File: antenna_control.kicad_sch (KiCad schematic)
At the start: 26 parts, among them J7 G125-MH11005L1P, J9 FTSH-105-01-L-DV-K, Q12 DMP2160UWQ-7, Q13 DMP3056LDM-7, U46 M0L1228QRGERQ1

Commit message: Add licensing
Use CERN-OHL-W version 2

Signed-off-by: Corey Minyard <corey@minyard.net>
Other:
- company: (none) -> AMSAT-NA
- title: (none) -> Processor for Interfaces to the Antenna Controller
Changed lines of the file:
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@@
 	(generator_version "10.0")
 	(paper "A4")
+	(title_block
+		(title "Processor for Interfaces to the Antenna Controller")
+		(date "2026-08-20")
+		(rev "4.0")
+		(company "AMSAT-NA")
+		(comment 1 "AE5KM")
+		(comment 2 "Copyright Corey Minyard, 2026")
+		(comment 3 "Licensed under CERN-OHL-W version 2")
+	)
 	(text "Can also be used as ADC channel 14 or BSL_Invoke"
 		(exclude_from_sim no)

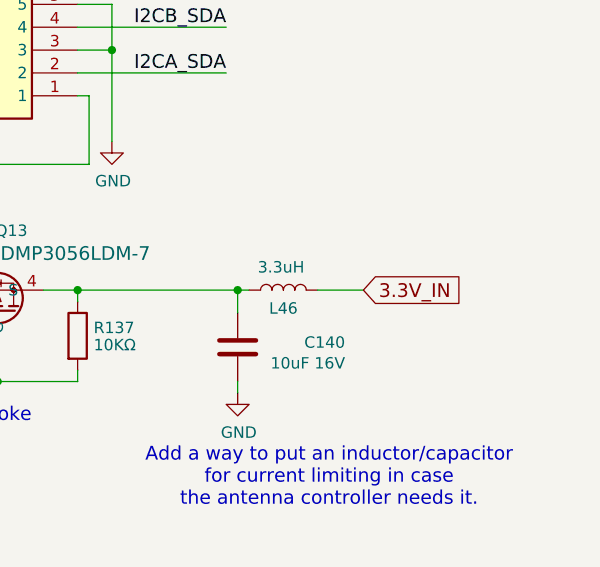
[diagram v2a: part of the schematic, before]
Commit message: Replace the metal allow inductors with ones that can be space-rated
Coilcraft had some space-rated and non-space-rated parts that had
equivalent footprints, which was handy.

Signed-off-by: Corey Minyard <corey@minyard.net>
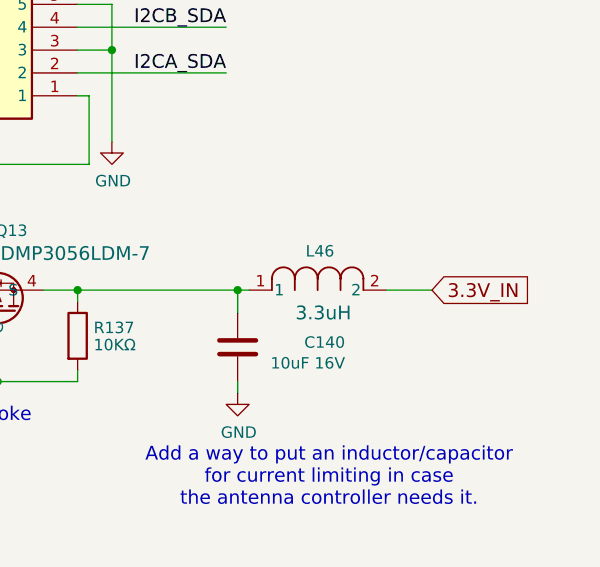
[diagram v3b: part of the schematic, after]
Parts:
- L46: footprint Inductor_SMD:L_1210_3225Metric_Pad1.42x2.65mm_HandSolder -> PacSatDev_misc:IND_EPL2010_COC; symbol Device:L -> PACSAT_DEV_misc:EPL2010
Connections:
- net 3.3V_IN: now also L46.2; no longer L46.1
- net at C140.1, Q13.4 (S), R137.1: now also L46.1; no longer L46.2
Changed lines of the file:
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@@
 	)
 	(junction
-		(at 247.65 68.58)
-		(diameter 0)
-		(color 0 0 0 0)
-	)
-	(junction
 		(at 134.62 137.16)
 		(diameter 0)
@@
 	)
 	(junction
+		(at 247.65 68.58)
+		(diameter 0)
+		(color 0 0 0 0)
+	)
+	(junction
 		(at 73.66 95.25)
 		(diameter 0)
@@
 	(wire
 		(pts
-			(xy 261.62 68.58) (xy 256.54 68.58)
+			(xy 269.24 68.58) (xy 264.16 68.58)
 		)
 		(stroke
@@
 	(global_label "3.3V_IN"
 		(shape input)
-		(at 261.62 68.58 0)
+		(at 269.24 68.58 0)
 		(fields_autoplaced yes)
 		(effects
@@
 		)
 		(property "Intersheetrefs" "${INTERSHEET_REFS}"
-			(at 272.835 68.58 0)
+			(at 280.455 68.58 0)
 			(hide yes)
 			(show_name no)
@@
 	)
 	(symbol
-		(lib_id "Device:L")
-		(at 252.73 68.58 270)
-		(mirror x)
+		(lib_id "PACSAT_DEV_misc:EPL2010")
+		(at 264.16 68.58 0)
+		(mirror y)
 		(unit 1)
 		(body_style 1)
@@
 		(dnp no)
 		(property "Reference" "L46"
-			(at 252.73 70.612 90)
+			(at 256.794 64.262 0)
 			(show_name no)
 			(do_not_autoplace no)
@@
 		)
 		(property "Value" "3.3uH"
-			(at 252.476 66.04 90)
+			(at 257.175 71.12 0)
 			(show_name no)
 			(do_not_autoplace no)
 			(effects
 				(font
-					(size 1.27 1.27)
+					(size 1.524 1.524)
 				)
 			)
 		)
-		(property "Footprint" "Inductor_SMD:L_1210_3225Metric_Pad1.42x2.65mm_HandSolder"
-			(at 252.73 68.58 0)
+		(property "Footprint" "PacSatDev_misc:IND_EPL2010_COC"
+			(at 264.16 68.58 0)
 			(hide yes)
 			(show_name no)
@@
 				(font
 					(size 1.27 1.27)
+					(italic yes)
 				)
 			)
 		)
-		(property "Datasheet" ""
-			(at 252.73 68.58 0)
+		(property "Datasheet" "https://www.coilcraft.com/getmedia/bdfddf40-0df1-48c7-a72c-6d6f57760a03/epl2010.pdf"
+			(at 264.16 68.58 0)
 			(hide yes)
 			(show_name no)
@@
 				(font
 					(size 1.27 1.27)
+					(italic yes)
 				)
 			)
 		)
 		(property "Description" ""
-			(at 252.73 68.58 0)
+			(at 264.16 68.58 0)
+			(hide yes)
 			(show_name no)
 			(do_not_autoplace no)

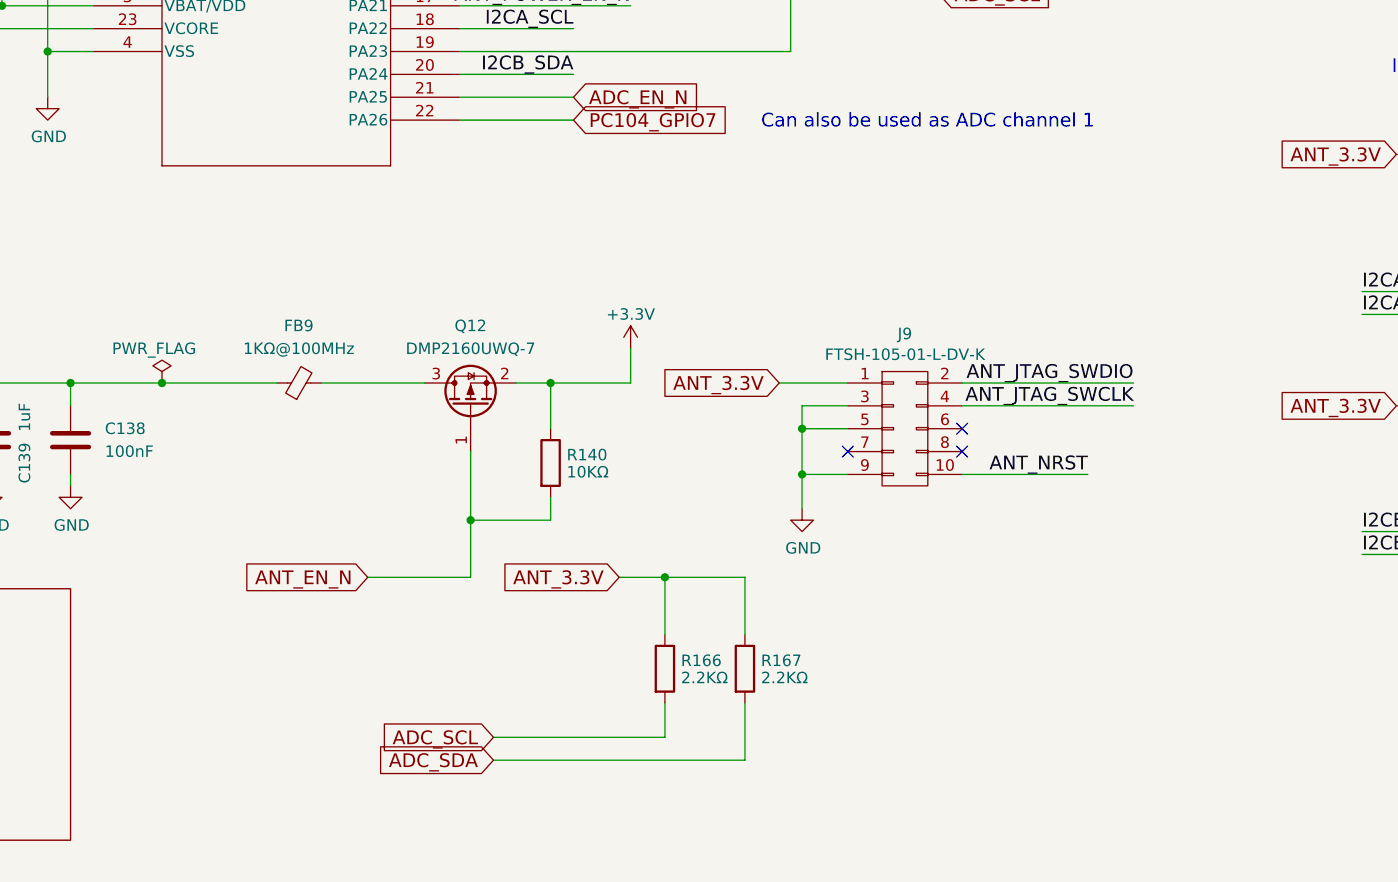
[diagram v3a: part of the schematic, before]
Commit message: Rework the antenna controller power
Change the MOSFET + ferrite to an inrush-controlled chip on the antenna
controller power and remove the separate ADC power enable.  Just power
the ADCs with the antenna controller power, there wasn't much benefit in
separate power control for it.

Signed-off-by: Corey Minyard <corey@minyard.net>
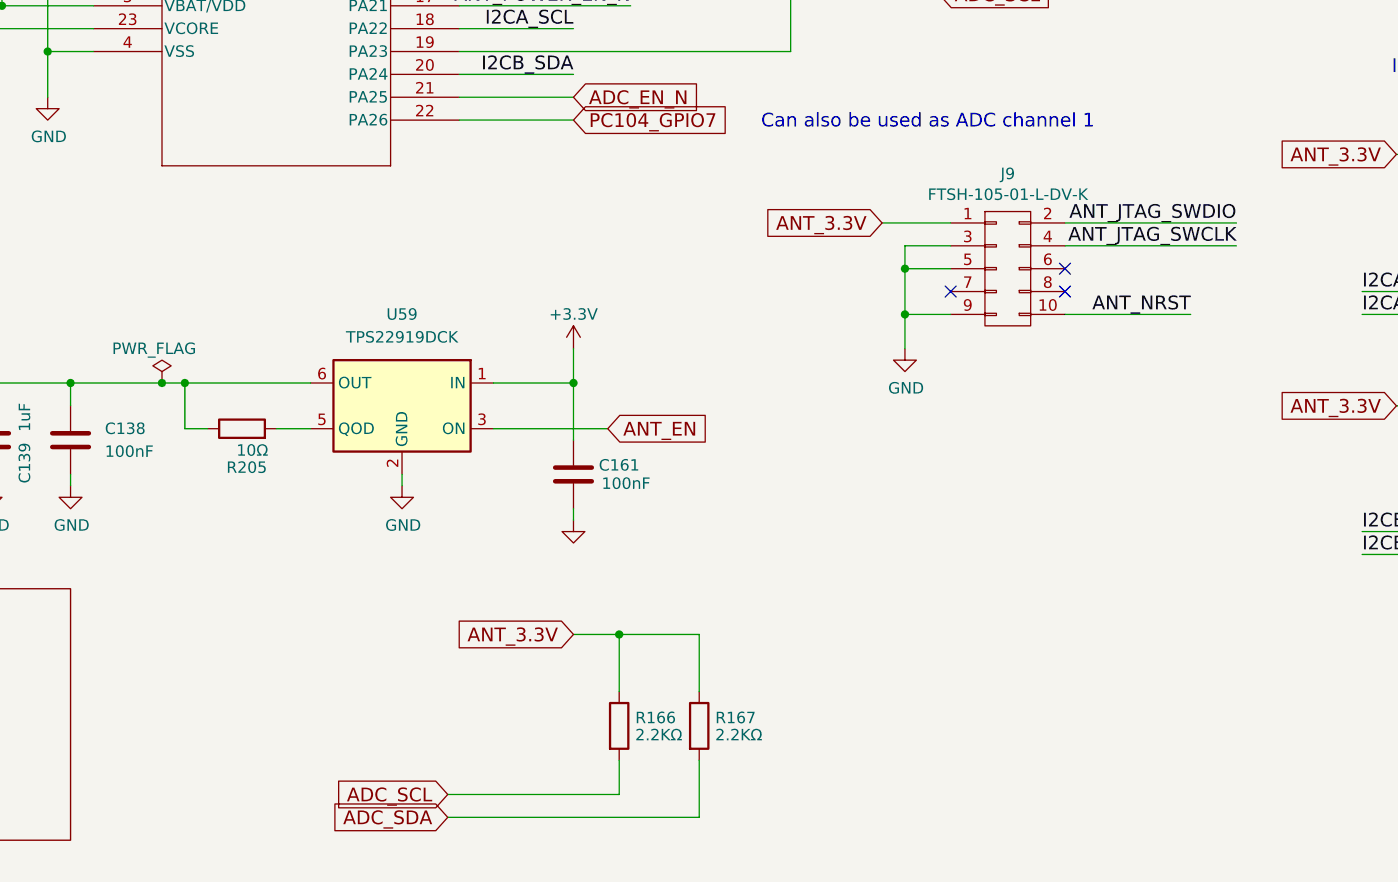
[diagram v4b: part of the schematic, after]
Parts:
- removed FB9: 1KΩ@100MHz, Inductor_SMD:L_0603_1608Metric_Pad1.05x0.95mm_HandSolder, symbol Device:FerriteBead_Small
- removed Q12: DMP2160UWQ-7, Package_TO_SOT_SMD:SOT-323_SC-70, symbol Transistor_FET:Q_PMOS_GSD
- removed R140: 10KΩ, Resistor_SMD:R_0402_1005Metric_Pad0.72x0.64mm_HandSolder, symbol Device:R
- added C161: 100nF, Capacitor_SMD:C_0402_1005Metric_Pad0.74x0.62mm_HandSolder, symbol Device:C
- added R205: 10Ω, Resistor_SMD:R_0402_1005Metric_Pad0.72x0.64mm_HandSolder, symbol Device:R
- added U59: TPS22919DCK, Package_TO_SOT_SMD:SOT-363_SC-70-6, symbol Power_Management:TPS22919DCK
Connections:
- net +3.3V: now also C161.1, U59.1 (IN)
- net ANT_3.3V: now also R205.1, U59.6 (OUT)
- net GND: now also C161.2, U59.2 (GND)
- new net: R205.2, U59.5 (QOD)
- new net ANT_EN: U59.3 (ON)
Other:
- moved on the sheet: J9, R166, R167

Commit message: Fix some missing BOM items
Signed-off-by: Corey Minyard <corey@minyard.net>
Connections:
- net ADC_EN_N renamed PC104_GPIO6
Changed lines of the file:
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@@
 		)
 	)
-	(global_label "ADC_EN_N"
+	(global_label "PC104_GPIO6"
 		(shape input)
 		(at 137.16 105.41 0)
@@
 		)
 		(property "Intersheetrefs" "${INTERSHEET_REFS}"
-			(at 151.2054 105.41 0)
+			(at 155.3418 105.41 0)
 			(hide yes)
 			(show_name no)

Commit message: Changed the USB connector
Changed to one that is raised and faces toward the RF section of the
board.  This will allow the connector to be used on the board as an
umbilical.  This required moving the RTC and a massive rework of the
entire USB section.

Signed-off-by: Corey Minyard <corey@minyard.net>
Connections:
- net PC104_GPIO8/ACP_BSL renamed PC104_GPIO8
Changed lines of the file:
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@@
 		)
 	)
-	(global_label "PC104_GPIO8{slash}ACP_BSL"
+	(global_label "PC104_GPIO8"
 		(shape input)
 		(at 130.81 82.55 0)
@@
 		)
 		(property "Intersheetrefs" "${INTERSHEET_REFS}"
-			(at 160.3129 82.55 0)
+			(at 148.9918 82.55 0)
 			(hide yes)
 			(show_name no)
@@
 		)
 	)
-	(global_label "PC104_GPIO8{slash}ACP_BSL"
+	(global_label "PC104_GPIO8"
 		(shape input)
 		(at 52.07 35.56 0)
@@
 		)
 		(property "Intersheetrefs" "${INTERSHEET_REFS}"
-			(at 81.5729 35.56 0)
-			(hide yes)
-			(show_name no)
+			(at 70.2518 35.56 0)
+			(hide yes)
+			(show_name no)

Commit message: Fix a few tracks and notes
Keep things out from under the RTC crystal, too.

Signed-off-by: Corey Minyard <corey@minyard.net>
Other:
- note removed: "Can also be used as ADC channel 14 or BSL_Invoke"
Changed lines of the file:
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@@
 		(comment 3 "Licensed under CERN-OHL-W version 2")
-	)
-	(text "Can also be used as ADC channel 14 or BSL_Invoke"
-		(exclude_from_sim no)
-		(at 197.866 82.55 0)
-		(effects
-			(font
-				(size 1.524 1.524)
-			)
-		)
 	)
 	(text "Add a way to put an inductor/capacitor\nfor current limiting in case\nthe antenna controller needs it."

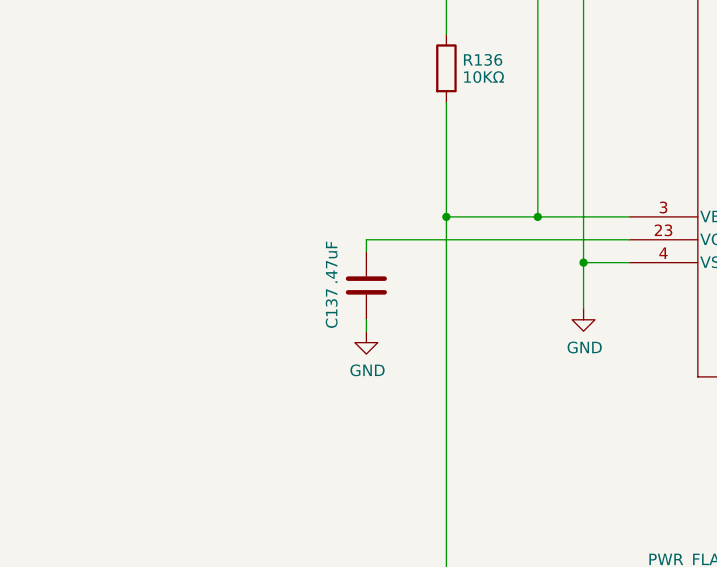
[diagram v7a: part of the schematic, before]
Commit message: Change all leading decimal points to 0.xxx
Improve readibility.

Also add some more BOM items.

Signed-off-by: Corey Minyard <corey@minyard.net>
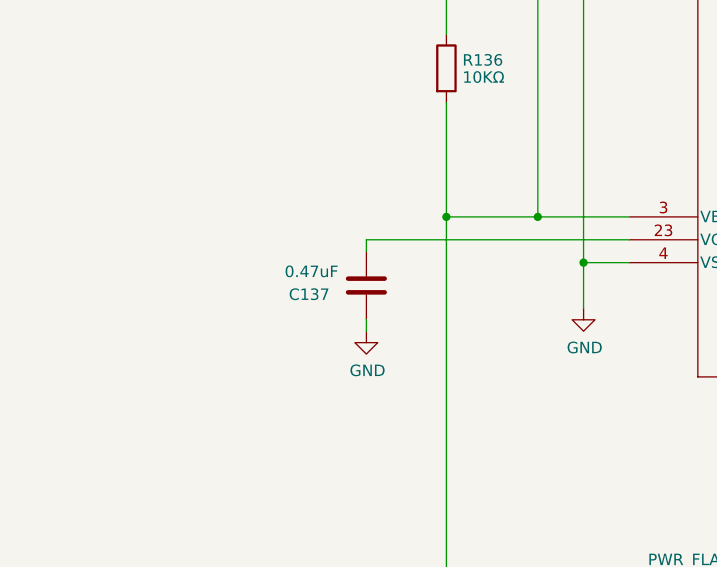
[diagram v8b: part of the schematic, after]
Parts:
- C137: value .47uF -> 0.47uF
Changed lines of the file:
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@@
 		(dnp no)
 		(property "Reference" "C137"
-			(at 50.8 105.41 90)
+			(at 48.26 103.886 0)
 			(show_name no)
 			(do_not_autoplace no)
@@
 			)
 		)
-		(property "Value" ".47uF"
-			(at 50.8 100.33 90)
+		(property "Value" "0.47uF"
+			(at 48.514 101.346 0)
 			(show_name no)
 			(do_not_autoplace no)
